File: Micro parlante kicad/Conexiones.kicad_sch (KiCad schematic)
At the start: 3 parts

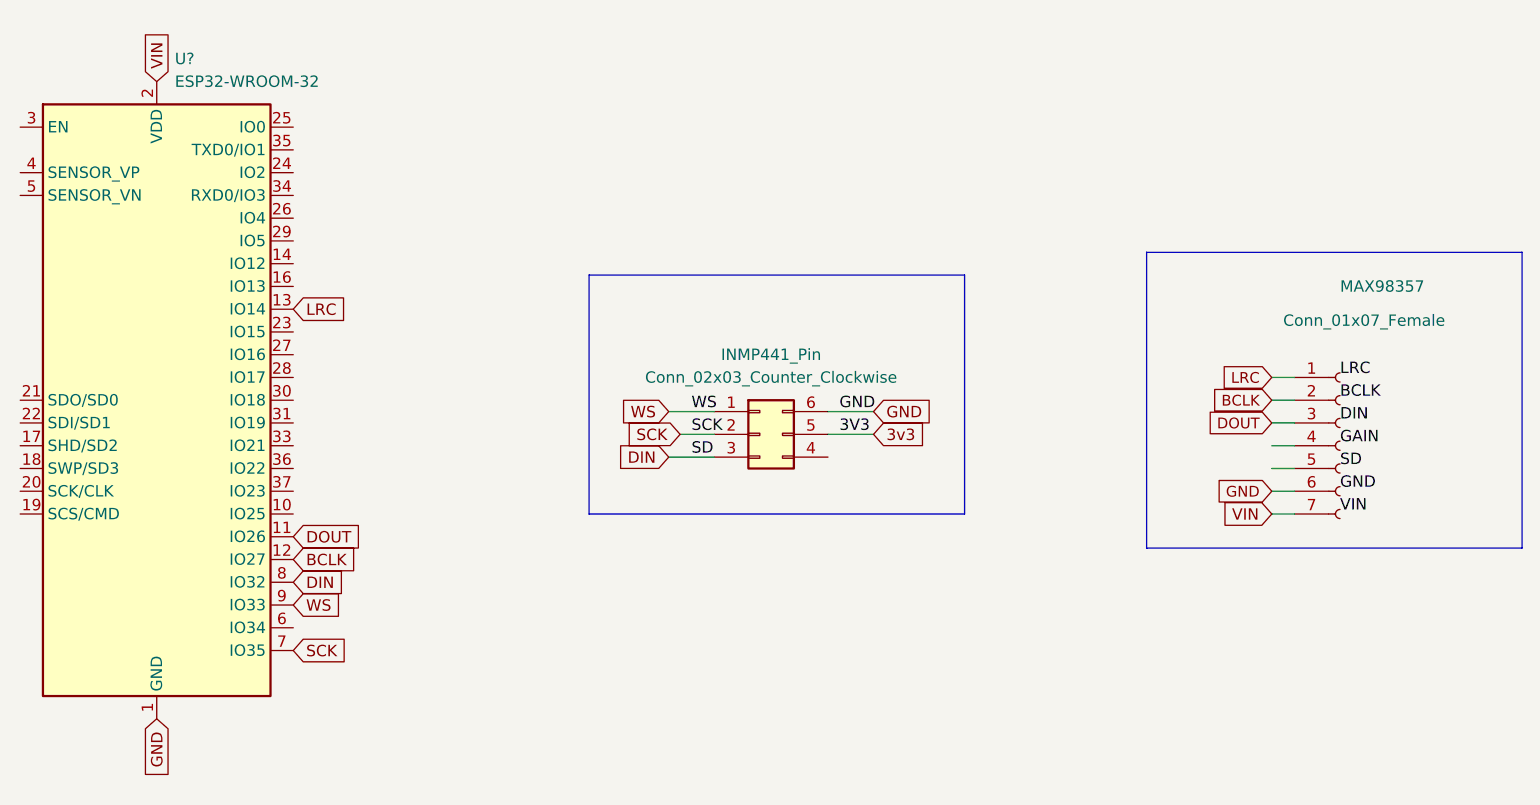
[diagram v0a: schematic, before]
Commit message: Unificación de relojes
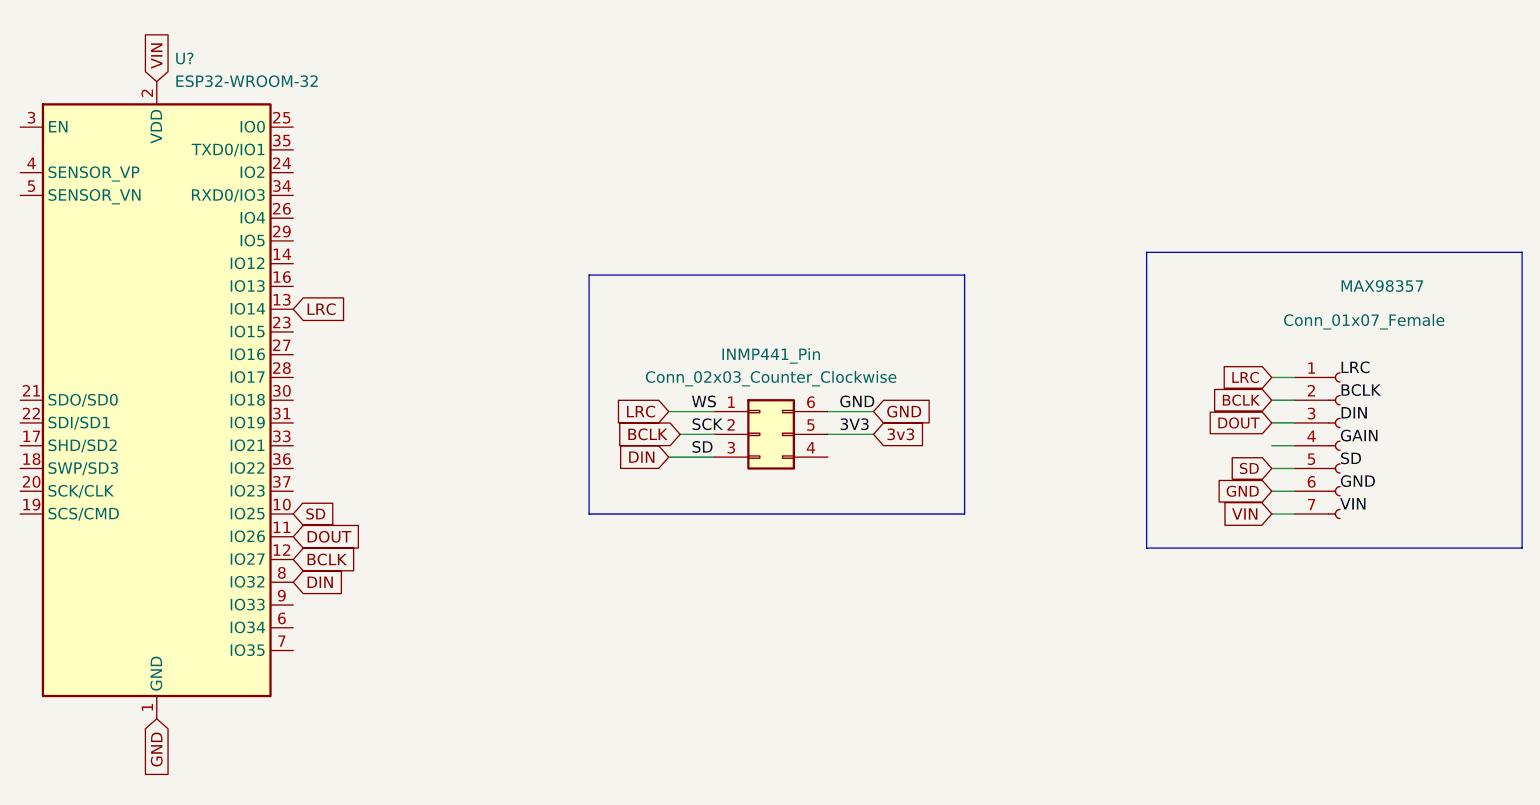
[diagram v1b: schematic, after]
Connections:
- net BCLK: now also INMP441_Pin.2 (Pin_2)
- net DIN: now also MAX98357.5 (Pin_5), U?.10 (IO25)
- net LRC: now also INMP441_Pin.1 (Pin_1)
- net SCK: no longer names the net of U?.7 (IO35)
- net SCK: no longer INMP441_Pin.2 (Pin_2)
- net WS: no longer names the net of U?.9 (IO33)
- net WS: no longer INMP441_Pin.1 (Pin_1)
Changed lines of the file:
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@@
     )
   )
-  (global_label "SCK" (shape input) (at 69.85 86.36 0) (fields_autoplaced)
-    (effects (font (size 1.27 1.27)) (justify left))
-    (property "Intersheet References" "${INTERSHEET_REFS}" (id 0) (at 76.0126 86.2806 0)
-      (effects (font (size 1.27 1.27)) (justify left) hide)
+  (global_label "SD" (shape input) (at 179.07 66.04 180) (fields_autoplaced)
+    (effects (font (size 1.2 1.2)) (justify right))
+    (property "Intersheet References" "${INTERSHEET_REFS}" (id 0) (at 174.4471 65.965 0)
+      (effects (font (size 1.2 1.2)) (justify right) hide)
     )
   )
-  (global_label "SCK" (shape input) (at 113.03 62.23 180) (fields_autoplaced)
+  (global_label "BCLK" (shape input) (at 113.03 62.23 180) (fields_autoplaced)
     (effects (font (size 1.27 1.27)) (justify right))
-    (property "Intersheet References" "${INTERSHEET_REFS}" (id 0) (at 106.8674 62.1506 0)
+    (property "Intersheet References" "${INTERSHEET_REFS}" (id 0) (at 105.7788 62.1506 0)
       (effects (font (size 1.27 1.27)) (justify right) hide)
     )
@@
     (effects (font (size 1.27 1.27)) (justify left))
     (property "Intersheet References" "${INTERSHEET_REFS}" (id 0) (at 77.1012 76.1206 0)
-      (effects (font (size 1.27 1.27)) (justify left) hide)
-    )
-  )
-  (global_label "WS" (shape input) (at 69.85 81.28 0) (fields_autoplaced)
-    (effects (font (size 1.27 1.27)) (justify left))
-    (property "Intersheet References" "${INTERSHEET_REFS}" (id 0) (at 74.9241 81.3594 0)
       (effects (font (size 1.27 1.27)) (justify left) hide)
     )
@@
     )
   )
+  (global_label "SD" (shape input) (at 69.85 71.12 0) (fields_autoplaced)
+    (effects (font (size 1.2 1.2)) (justify left))
+    (property "Intersheet References" "${INTERSHEET_REFS}" (id 0) (at 74.4729 71.195 0)
+      (effects (font (size 1.2 1.2)) (justify left) hide)
+    )
+  )
   (global_label "GND" (shape input) (at 134.62 59.69 0) (fields_autoplaced)
     (effects (font (size 1.27 1.27)) (justify left))
@@
     )
   )
-  (global_label "WS" (shape input) (at 111.76 59.69 180) (fields_autoplaced)
+  (global_label "LRC" (shape input) (at 111.76 59.69 180) (fields_autoplaced)
     (effects (font (size 1.27 1.27)) (justify right))
-    (property "Intersheet References" "${INTERSHEET_REFS}" (id 0) (at 106.6859 59.6106 0)
+    (property "Intersheet References" "${INTERSHEET_REFS}" (id 0) (at 105.7788 59.6106 0)
       (effects (font (size 1.27 1.27)) (justify right) hide)
     )
